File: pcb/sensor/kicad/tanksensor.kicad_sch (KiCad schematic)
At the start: 16 parts, among them J1 43045-0600, U1 FDC1004DGSR, U2 TPS7A2433DBVR, U3 ESDS312DBVR

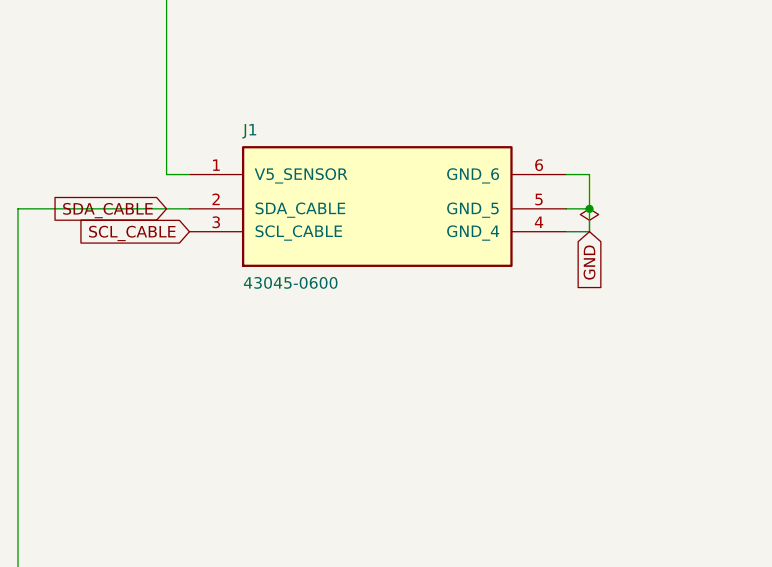
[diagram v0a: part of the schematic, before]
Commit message: Prepare compact three-board designs for owner routing
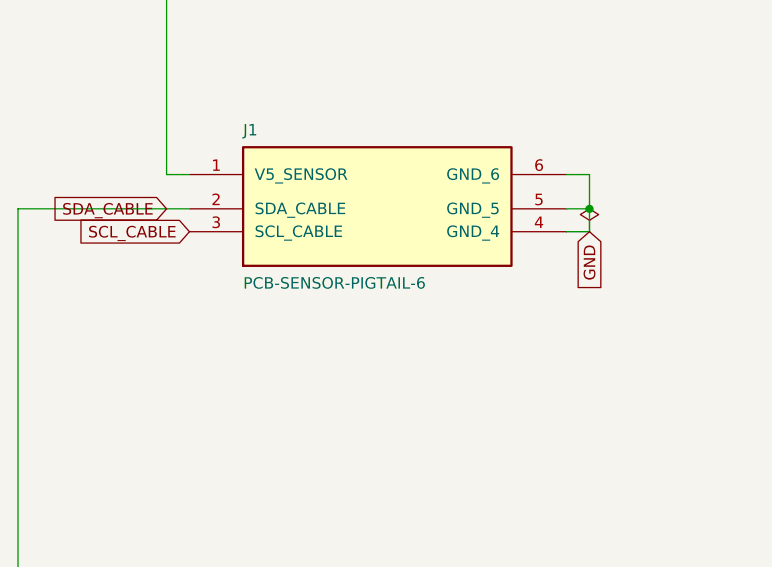
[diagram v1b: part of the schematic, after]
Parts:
- J1: value 43045-0600 -> PCB-SENSOR-PIGTAIL-6; MPN 43045-0600 -> PCB-SENSOR-PIGTAIL-6; now left out of the parts list
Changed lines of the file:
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@@
 		(body_style 1)
 		(exclude_from_sim no)
-		(in_bom yes)
+		(in_bom no)
 		(on_board yes)
-		(in_pos_files yes)
+		(in_pos_files no)
 		(dnp no)
 		(property "Reference" "J1"
@@
 			)
 		)
-		(property "Value" "43045-0600"
+		(property "Value" "PCB-SENSOR-PIGTAIL-6"
 			(at 185.0335 189.8858 0)
 			(show_name no)
@@
 			)
 		)
-		(property "Datasheet" "https://www.molex.com/content/dam/molex/molex-dot-com/products/automated/en-us/salesdrawingpdf/430/43045/430450600_sd.pdf"
-			(at 199.39 181.61 0)
+		(property "Datasheet" ""
+			(at 0 0 0)
 			(hide yes)
 			(show_name no)
@@
 			)
 		)
-		(property "Description" "Integrated Circuit"
-			(at 199.39 181.61 0)
-			(hide yes)
-			(show_name no)
-			(do_not_autoplace no)
-			(effects
-				(font
-					(size 1.27 1.27)
-				)
-			)
-		)
-		(property "MPN" "43045-0600"
+		(property "Description" "Six solder pads for left-exiting sensor pigtail"
 			(at 199.39 181.61 0)
 			(hide yes)
@@
 			(hide yes)
 			(show_name no)
+			(do_not_autoplace no)
+			(effects
+				(font
+					(size 1.27 1.27)
+				)
+			)
+		)
+		(property "MPN" "PCB-SENSOR-PIGTAIL-6"
+			(at 0 0 0)
+			(hide yes)
+			(show_name no)
